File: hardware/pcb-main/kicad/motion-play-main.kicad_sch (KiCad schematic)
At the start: 24 parts, among them J2 DWEII Power Module, J3 LED_Strip, J4 Conn_01x05, J5 Conn_01x05, J6 Conn_01x05, U1 AP2112K-3.3TRG1, U2 T-Display-S3

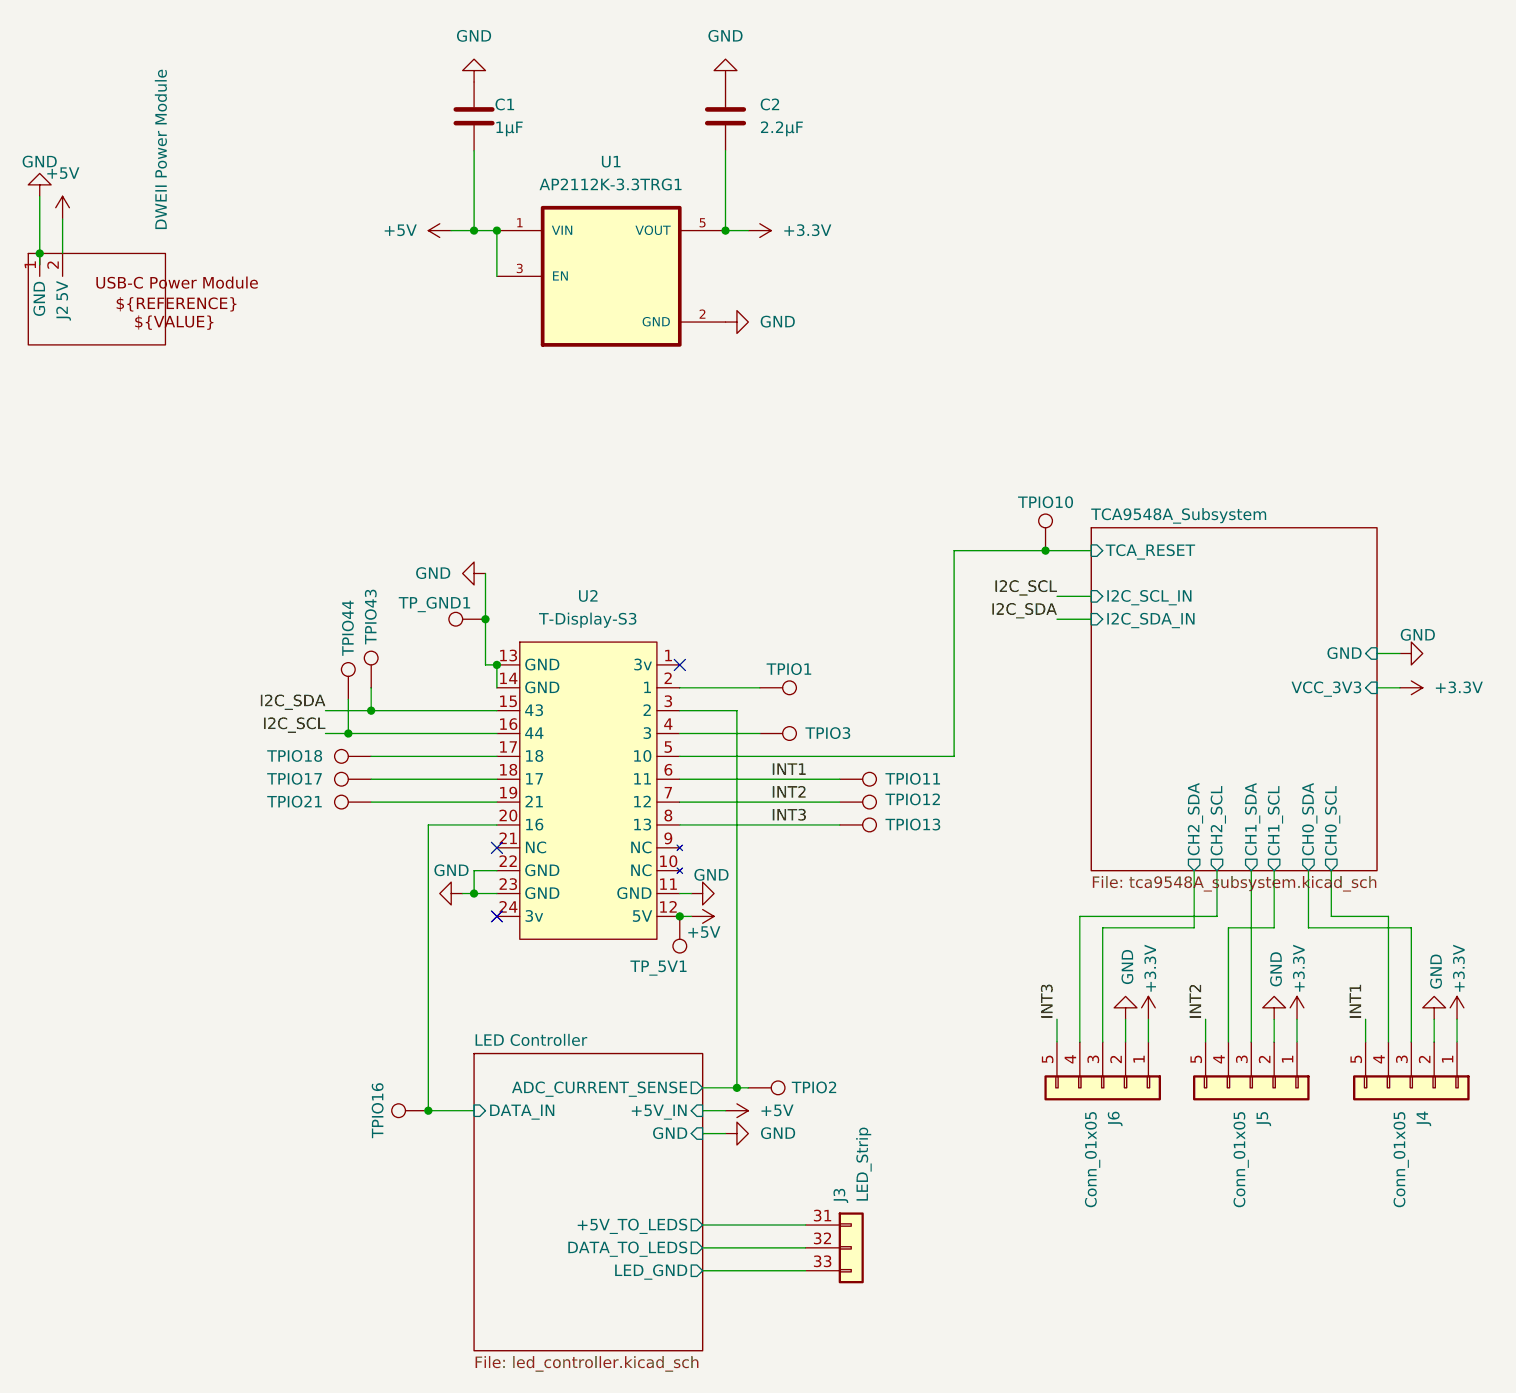
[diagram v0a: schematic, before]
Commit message: Finished sensor redesign
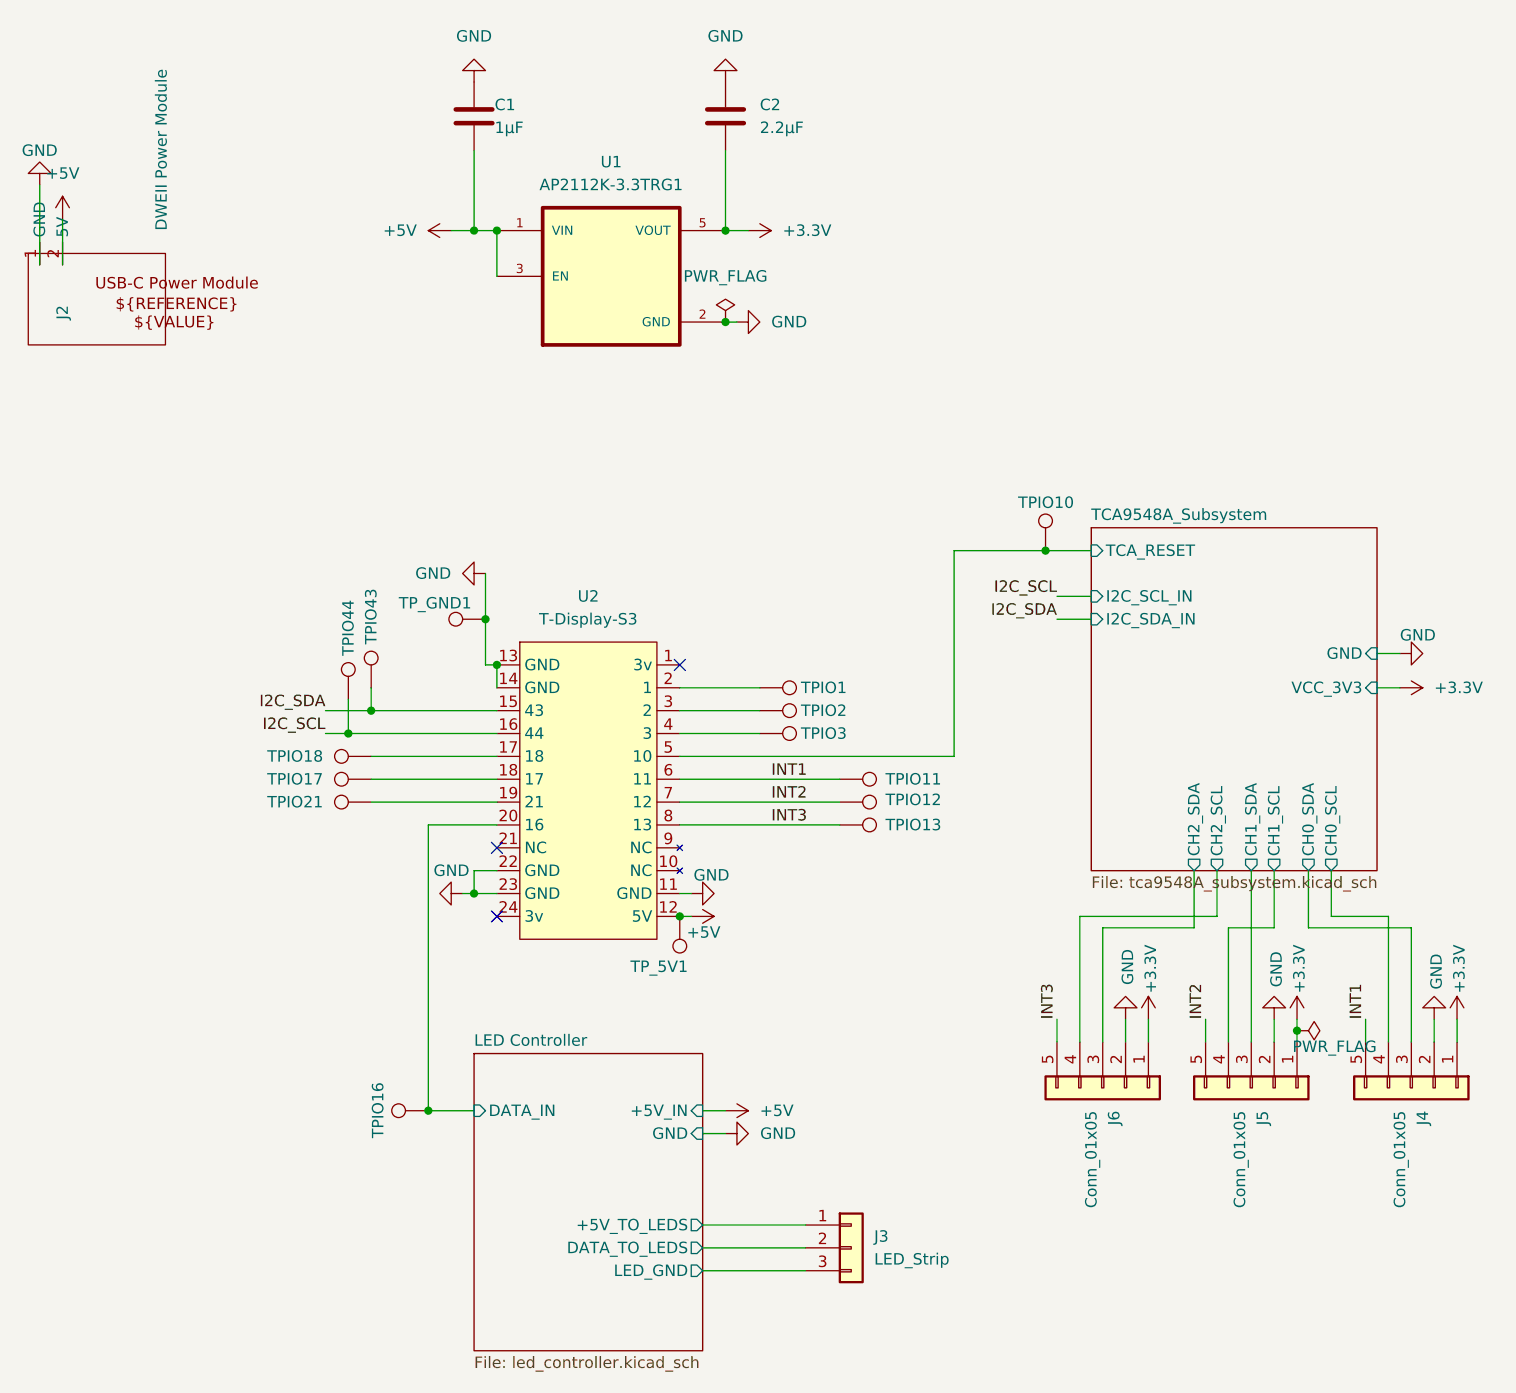
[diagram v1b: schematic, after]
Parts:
- J2: footprint Library:USBC_Power_Module -> motion-play-footprints:USBC_Power_Module; symbol motion-play_Library:USBC_Power_Module -> motion-play-symbols:USBC_Power_Module
- J3: footprint Connector_JST:JST_XH_B3B-XH-AM_1x03_P2.50mm_Vertical -> Connector_JST:JST_PH_S3B-PH-SM4-TB_1x03-1MP_P2.00mm_Horizontal
- J4, J5, J6: footprint (none) -> Connector_JST:JST_SH_SM05B-SRSS-TB_1x05-1MP_P1.00mm_Horizontal
- U1: footprint AP2112K-3.3TRG1:SOT95P285X140-5N -> motion-play-footprints:SOT95P285X140-5N
- U2: footprint Library:T-Display-S3 -> motion-play-footprints:T-Display-S3; symbol T-Display-S3:T-Display-S3 -> motion-play-symbols:T-Display-S3; now in the parts list
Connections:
- net LED Controller/+5V_TO_LEDS: now also J3.1 (Pin_1); no longer J3.31 (Pin_1)
- net LED Controller/DATA_TO_LEDS: now also J3.2 (Pin_2); no longer J3.32 (Pin_2)
- net LED Controller/LED_GND: now also J3.3 (Pin_3); no longer J3.33 (Pin_3)
- net LED Controller/ADC_CURRENT_SENSE: no longer names the net of TPIO2.1, U2.3 (2)
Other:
- sheet LED Controller ports: added none; removed ADC_CURRENT_SENSE
- moved on the sheet: J2, TPIO2

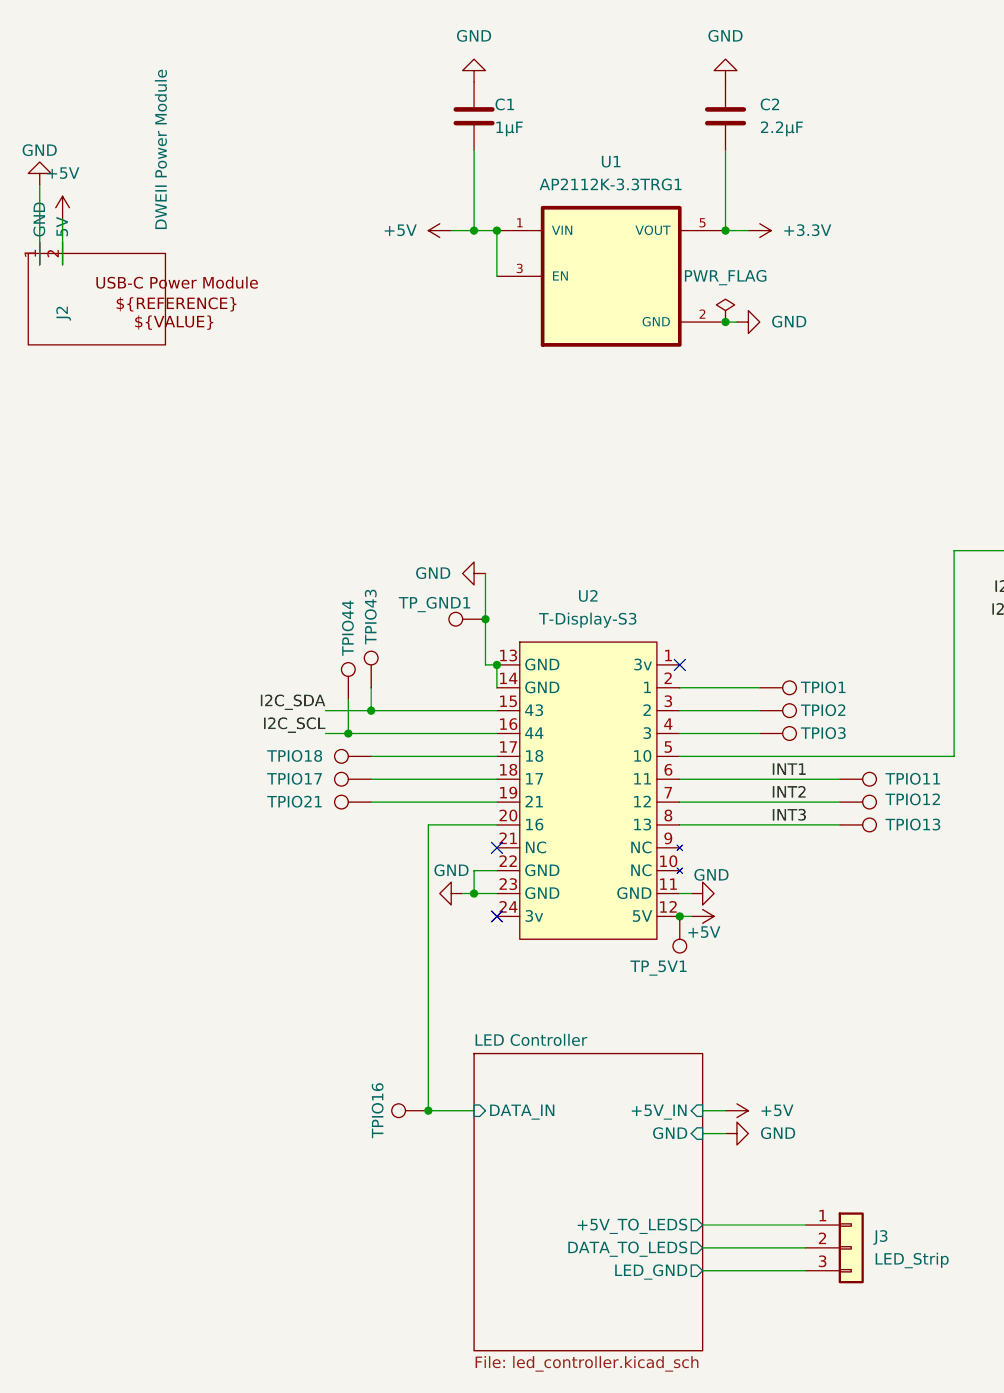
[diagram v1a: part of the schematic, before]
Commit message: Proximity detection and updated pcbs
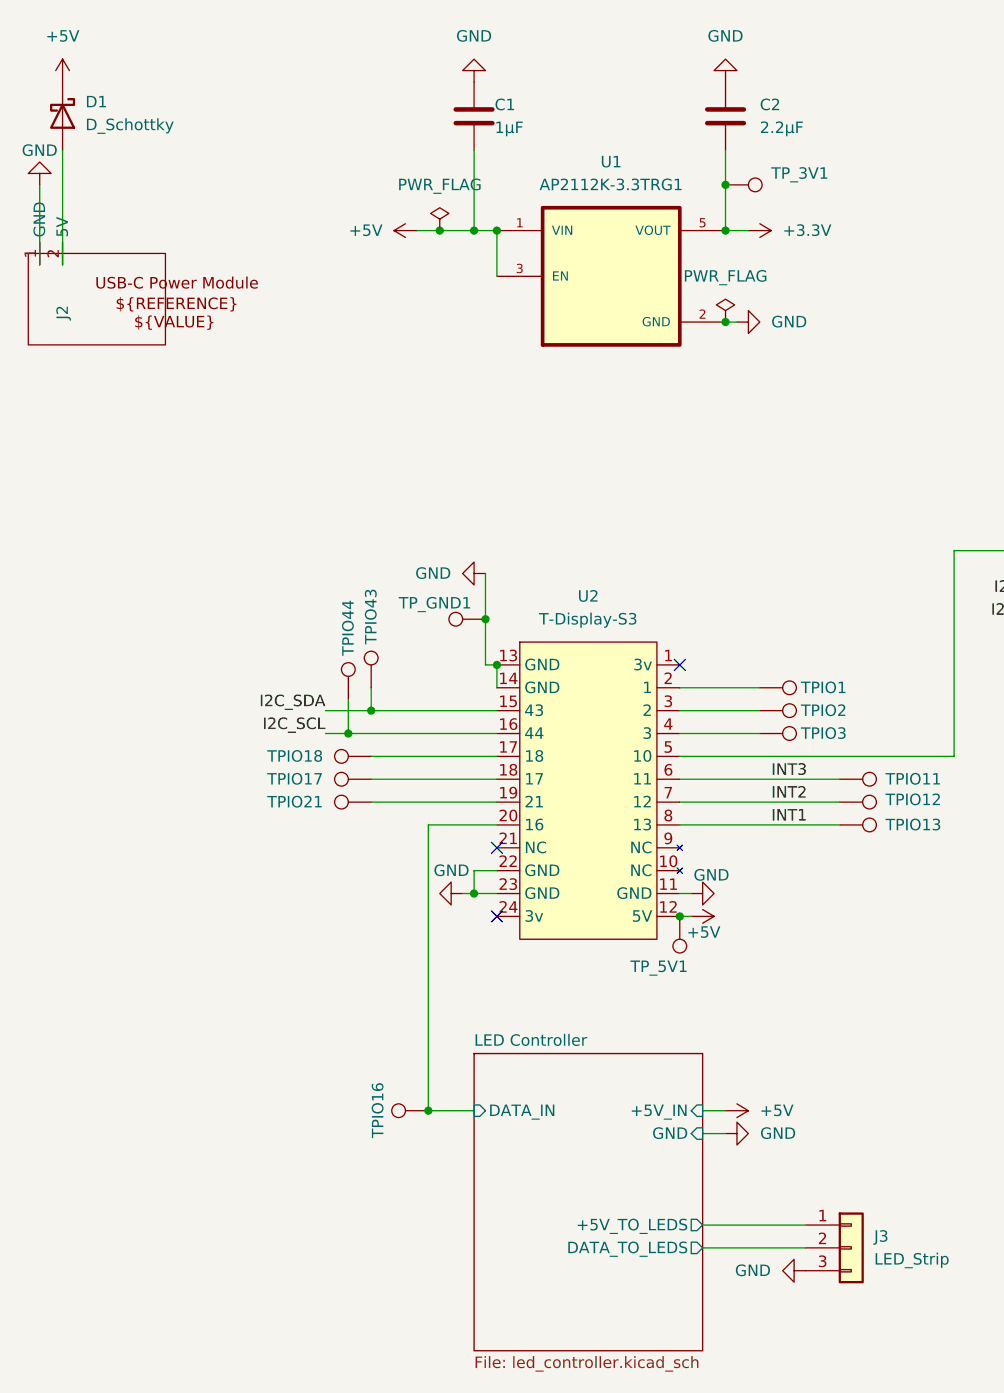
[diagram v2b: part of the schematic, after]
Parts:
- added D1: D_Schottky, Diode_SMD:D_SMC, symbol Device:D_Schottky
- added TP_3V1: TestPoint, TestPoint:TestPoint_Pad_D2.0mm, symbol Connector:TestPoint
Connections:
- net LED Controller/LED_GND is gone; now on net GND: J3.3 (Pin_3)
- net +3.3V: now also TP_3V1.1
- net +5V: now also D1.1 (K); no longer J2.2 (5V)
- net INT1: now also TPIO13.1, U2.8 (13); no longer TPIO11.1, U2.6 (11)
- net INT3: now also TPIO11.1, U2.6 (11); no longer TPIO13.1, U2.8 (13)
- new net: D1.2 (A), J2.2 (5V)
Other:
- sheet LED Controller ports: added none; removed LED_GND
